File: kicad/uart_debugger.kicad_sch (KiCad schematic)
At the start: 1 part, among them J3 Conn_01x03

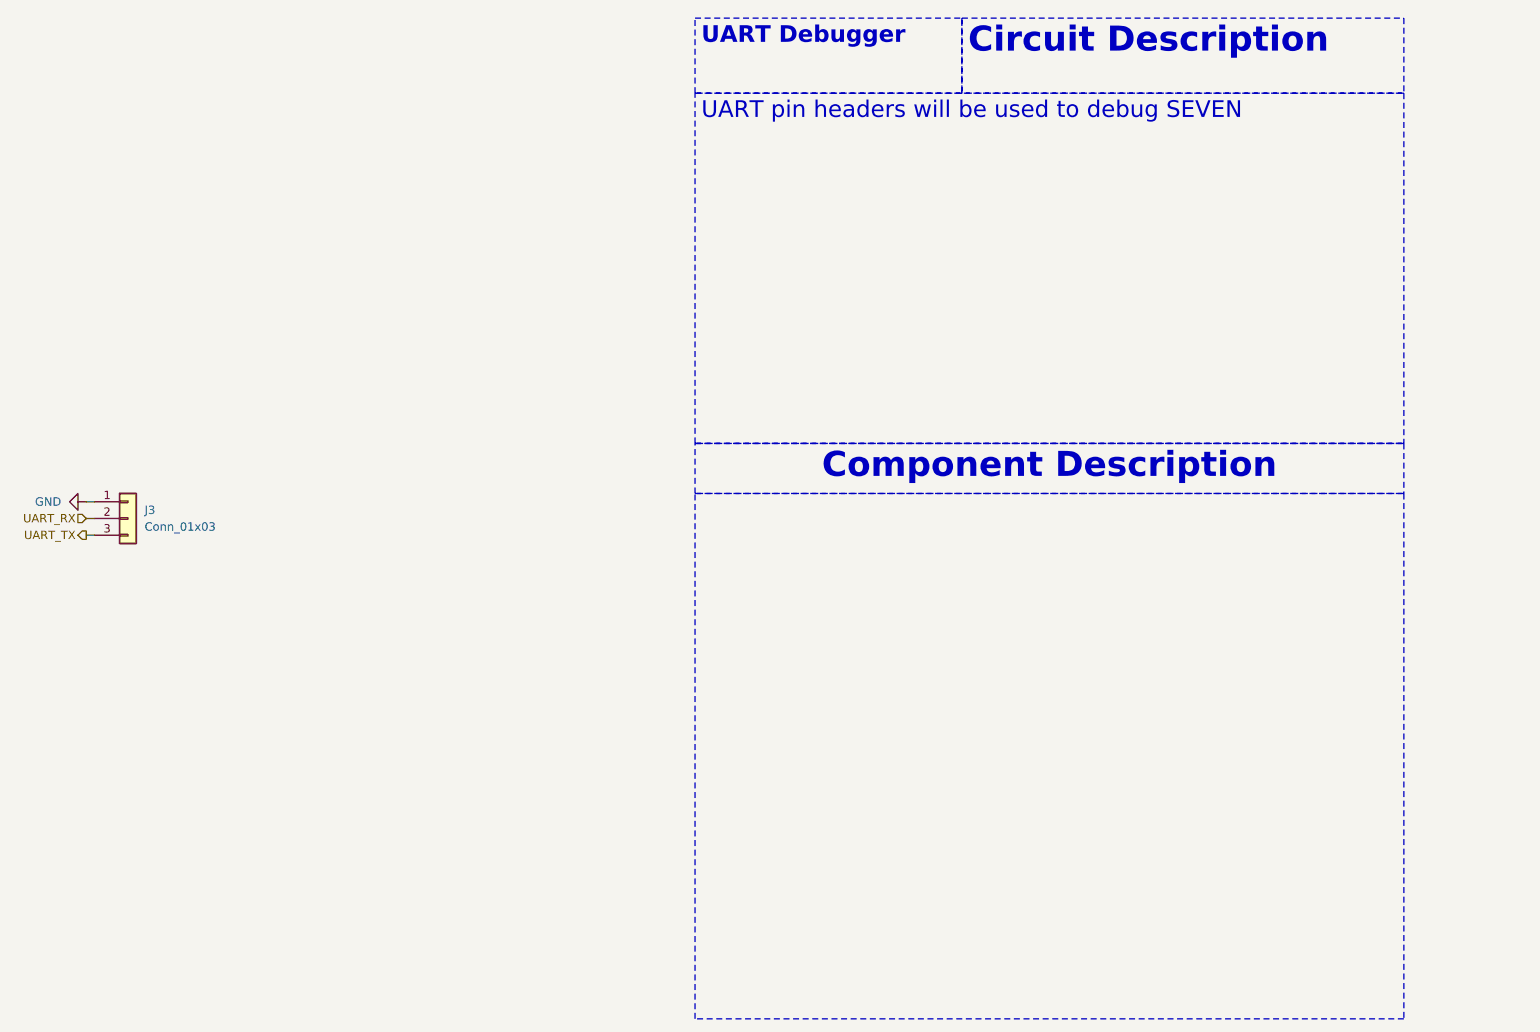
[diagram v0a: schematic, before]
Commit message: docs: update documentation to be more accurate
Signed-off-by: Bobo Bäck Engström <bobo@id8-engineering.io>
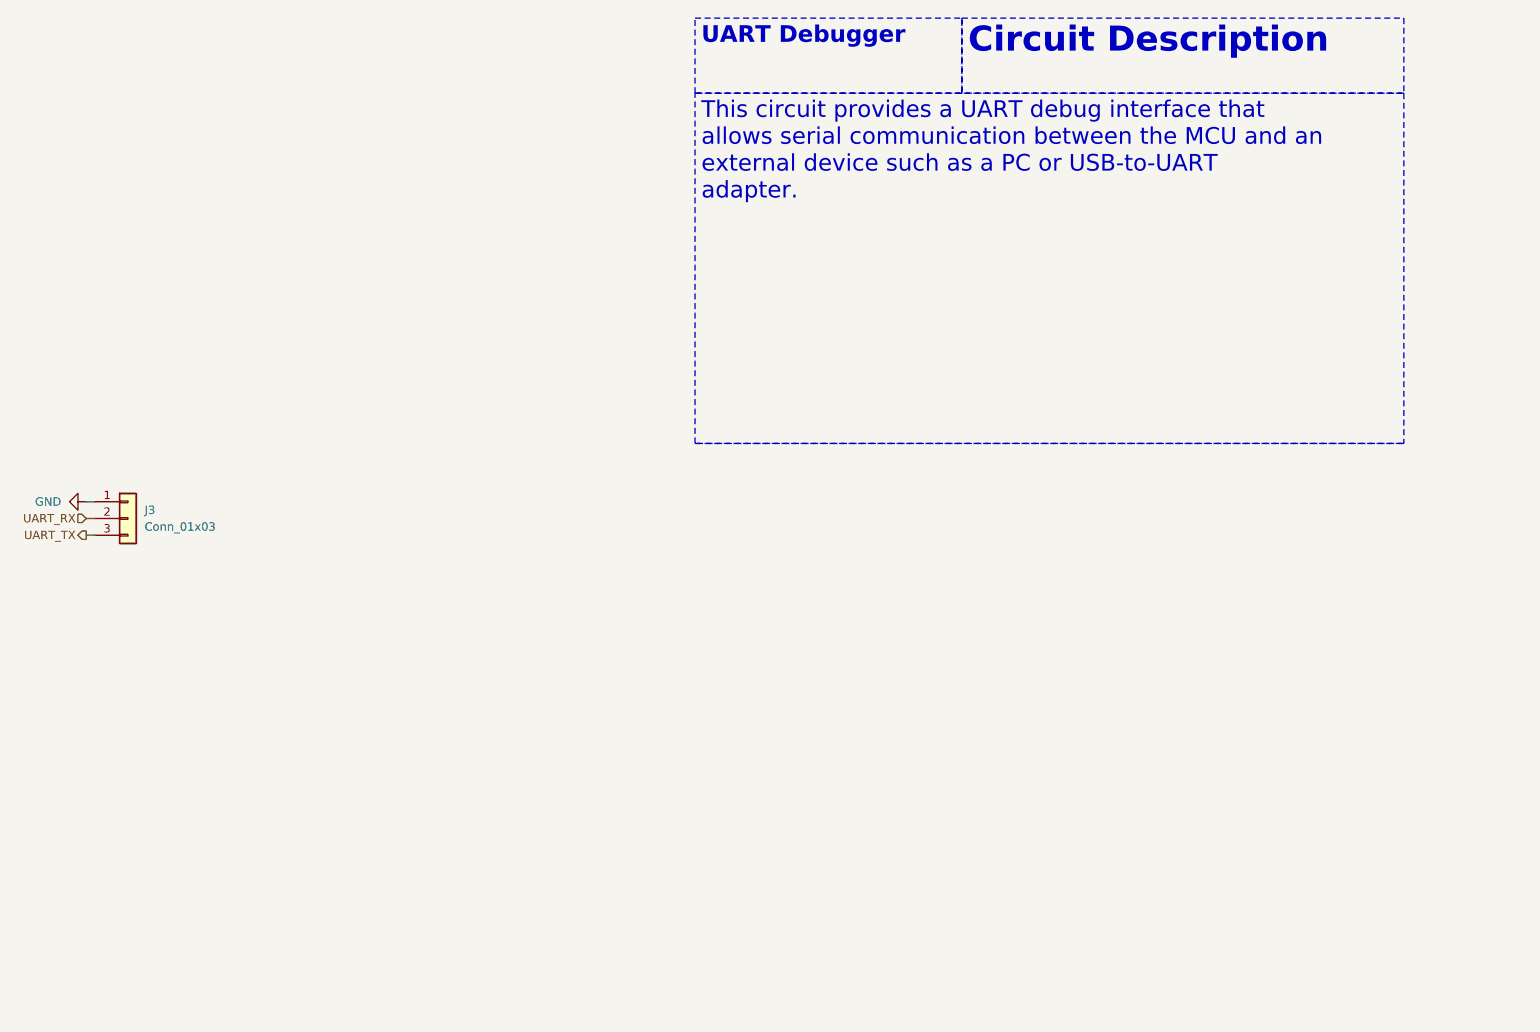
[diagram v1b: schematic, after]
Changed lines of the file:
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@@
 		)
 	)
-	(text_box "UART pin headers will be used to debug SEVEN"
+	(text_box "This circuit provides a UART debug interface that allows serial communication between the MCU and an external device such as a PC or USB-to-UART adapter."
 		(exclude_from_sim no)
 		(at 176.53 24.13 0)
 		(size 107.95 53.34)
-		(margins 0.9525 0.9525 0.9525 0.9525)
-		(stroke
-			(width 0)
-			(type dash)
-		)
-		(fill
-			(type none)
-		)
-		(effects
-			(font
-				(size 2.54 2.54)
-			)
-			(justify left top)
-		)
-	)
-	(text_box "\n"
-		(exclude_from_sim no)
-		(at 176.53 85.09 0)
-		(size 107.95 80.01)
 		(margins 0.9525 0.9525 0.9525 0.9525)
 		(stroke
@@
 		)
 	)
-	(text_box "Component Description\n"
-		(exclude_from_sim no)
-		(at 176.53 77.47 0)
-		(size 107.95 7.62)
-		(margins 0.9525 0.9525 0.9525 0.9525)
-		(stroke
-			(width 0)
-			(type dash)
-		)
-		(fill
-			(type none)
-		)
-		(effects
-			(font
-				(size 3.81 3.81)
-				(thickness 0.762)
-				(bold yes)
-			)
-			(justify top)
-		)
-	)

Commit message: feat: add jumper to VDD_GPIO to expose either 1V8 or 3V3
Signed-off-by: Bobo Bäck Engström <bobo@id8-engineering.io>
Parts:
- J3: footprint seven-lib:PinHeader_1x03_P1.00mm_Vertical_SMD_Pin1Left -> seven-lib:PinHeader_1x03_P2.54mm_Vertical_SMD_Pin1Left
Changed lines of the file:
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@@
 			)
 		)
-		(property "Footprint" "seven-lib:PinHeader_1x03_P1.00mm_Vertical_SMD_Pin1Left"
+		(property "Footprint" "seven-lib:PinHeader_1x03_P2.54mm_Vertical_SMD_Pin1Left"
 			(at 90.17 88.9 0)
 			(effects

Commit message: feat(PCB): set component-placement example on PCB
This pr will fail due to DRC, skip this and lets have a conversation
about the placement only

Signed-off-by: Bobo Bäck Engström <bobo@id8-engineering.io>
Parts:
- J3: LCSC (none) -> C5988151; MPN (none) -> M20-8770342
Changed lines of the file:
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@@
 (kicad_sch
-	(version 20250114)
+	(version 20260306)
 	(generator "eeschema")
-	(generator_version "9.0")
+	(generator_version "10.0")
 	(paper "A4")
 	(text "\n\n"
@@
 		(at 90.17 88.9 0)
 		(unit 1)
+		(body_style 1)
 		(exclude_from_sim no)
 		(in_bom yes)
 		(on_board yes)
+		(in_pos_files yes)
 		(dnp no)
 		(fields_autoplaced yes)
 		(property "Reference" "J3"
 			(at 92.71 87.6299 0)
+			(show_name no)
+			(do_not_autoplace no)
 			(effects
 				(font
@@
 		(property "Value" "Conn_01x03"
 			(at 92.71 90.1699 0)
+			(show_name no)
+			(do_not_autoplace no)
 			(effects
 				(font
@@
 		(property "Footprint" "seven-lib:PinHeader_1x03_P2.54mm_Vertical_SMD_Pin1Left"
 			(at 90.17 88.9 0)
-			(effects
-				(font
-					(size 1.27 1.27)
-				)
-				(hide yes)
-			)
-		)
-		(property "Datasheet" "~"
-			(at 90.17 88.9 0)
-			(effects
-				(font
-					(size 1.27 1.27)
-				)
-				(hide yes)
+			(hide yes)
+			(show_name no)
+			(do_not_autoplace no)
+			(effects
+				(font
+					(size 1.27 1.27)
+				)
+			)
+		)
+		(property "Datasheet" "https://content.harwin.com/m/847482046069c548/original/PD008-Product-Datasheet-INDESS-range-M20-and-M22-BBi.pdf"
+			(at 90.17 88.9 0)
+			(hide yes)
+			(show_name no)
+			(do_not_autoplace no)
+			(effects
+				(font
+					(size 1.27 1.27)
+				)
 			)
 		)
 		(property "Description" "Generic connector, single row, 01x03, script generated (kicad-library-utils/schlib/autogen/connector/)"
 			(at 90.17 88.9 0)
-			(effects
-				(font
-					(size 1.27 1.27)
-				)
-				(hide yes)
+			(hide yes)
+			(show_name no)
+			(do_not_autoplace no)
+			(effects
+				(font
+					(size 1.27 1.27)
+				)
+			)
+		)
+		(property "LCSC" "C5988151"
+			(at 90.17 88.9 0)
+			(hide yes)
+			(show_name no)
+			(do_not_autoplace no)
+			(effects
+				(font
+					(size 1.27 1.27)
+				)
+			)
+		)
+		(property "MPN" "M20-8770342"
+			(at 90.17 88.9 0)
+			(hide yes)
+			(show_name no)
+			(do_not_autoplace no)
+			(effects
+				(font
+					(size 1.27 1.27)
+				)
+			)
+		)
+		(property "Manufacturer Part Number" ""
+			(at 90.17 88.9 0)
+			(hide yes)
+			(show_name no)
+			(do_not_autoplace no)
+			(effects
+				(font
+					(size 1.27 1.27)
+				)
 			)
 		)
@@
 		)
 		(instances
-			(project ""
+			(project "seven"
 				(path "/8e3cc843-5797-49f3-8b3a-1c11450ccd1e/bfb076a8-082c-4e75-8c21-42e3541223ce"
 					(reference "J3")
@@
 		(at 83.82 86.36 270)
 		(unit 1)
+		(body_style 1)
 		(exclude_from_sim no)
 		(in_bom yes)
 		(on_board yes)
+		(in_pos_files yes)
 		(dnp no)
 		(fields_autoplaced yes)
 		(property "Reference" "#PWR06"
 			(at 77.47 86.36 0)
-			(effects
-				(font
-					(size 1.27 1.27)
-				)
-				(hide yes)
+			(hide yes)
+			(show_name no)
+			(do_not_autoplace no)
+			(effects
+				(font
+					(size 1.27 1.27)
+				)
 			)
 		)
 		(property "Value" "GND"
 			(at 80.01 86.3599 90)
+			(show_name no)
+			(do_not_autoplace no)
 			(effects
 				(font
@@
 		(property "Footprint" ""
 			(at 83.82 86.36 0)
-			(effects
-				(font
-					(size 1.27 1.27)
-				)
-				(hide yes)
+			(hide yes)
+			(show_name no)
+			(do_not_autoplace no)
+			(effects
+				(font
+					(size 1.27 1.27)
+				)
 			)
 		)
 		(property "Datasheet" ""
 			(at 83.82 86.36 0)
-			(effects
-				(font
-					(size 1.27 1.27)
-				)
-				(hide yes)
+			(hide yes)
+			(show_name no)
+			(do_not_autoplace no)
+			(effects
+				(font
+					(size 1.27 1.27)
+				)
 			)
 		)
 		(property "Description" "Power symbol creates a global label with name \"GND\" , ground"
 			(at 83.82 86.36 0)
-			(effects
-				(font
-					(size 1.27 1.27)
-				)
-				(hide yes)
+			(hide yes)
+			(show_name no)
+			(do_not_autoplace no)
+			(effects
+				(font
+					(size 1.27 1.27)
+				)
 			)
 		)
@@
 		)
 		(instances
-			(project ""
+			(project "seven"
 				(path "/8e3cc843-5797-49f3-8b3a-1c11450ccd1e/bfb076a8-082c-4e75-8c21-42e3541223ce"
 					(reference "#PWR06")
